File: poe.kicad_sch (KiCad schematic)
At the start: 59 parts, among them IC1 TPS2378DDA, J1 B2B-XH-A_LF__SN_, J6 SS-74800-144, U3 TPS2373-3RGW, U4 URB4805YMD-30WR3

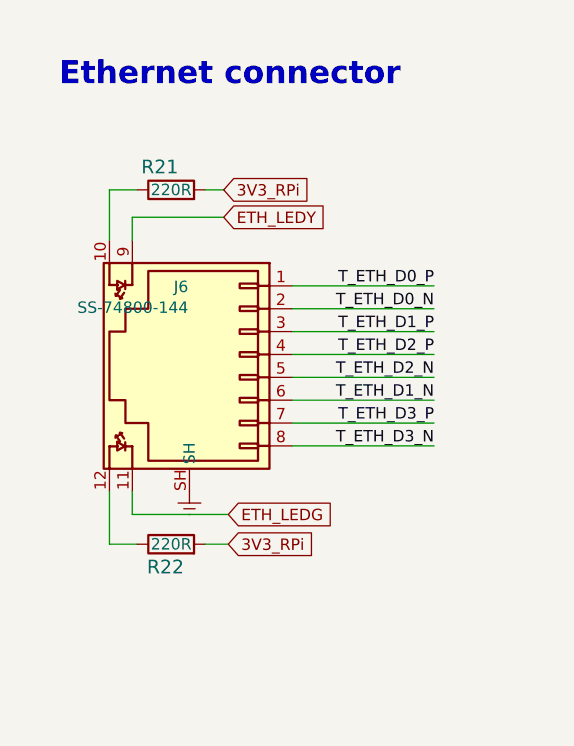
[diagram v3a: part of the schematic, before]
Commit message: Update R21, R22, R56, R57, R60, R61 symbol and footprints
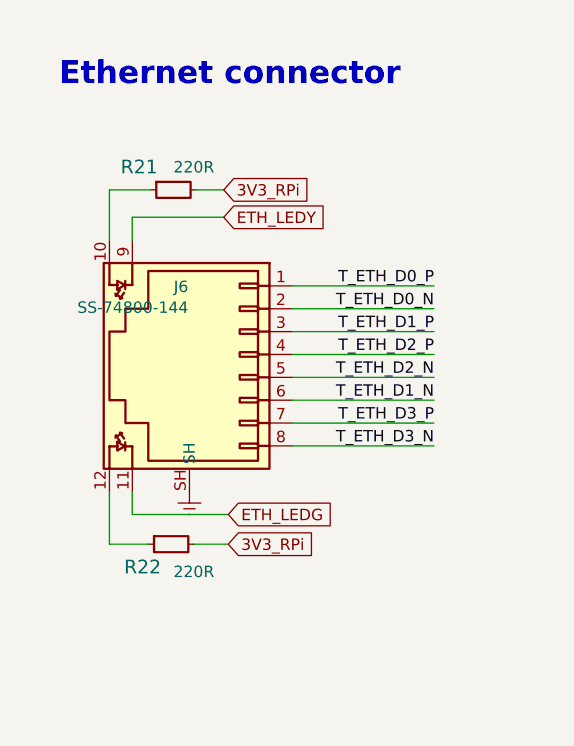
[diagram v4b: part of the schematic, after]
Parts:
- R21, R22: footprint scalenode-cm4-baseboard-footprints:0402-res -> antmicro-footprints:R_0402_1005Metric; symbol scalenode-cm4-baseboard:R_220R_0402 -> antmicroResistors0402:R_220R_0402; Author (none) -> Antmicro; License (none) -> Apache-2.0; MPN ERJ2GEJ221X -> CR0402-FX-2200GLF; Manufacturer Panasonic -> Bourns; Tolerance (none) -> 1%
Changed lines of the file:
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@@
     (stroke (width 0) (type default) (color 0 0 0 0))
   )
-  (wire (pts (xy 53.594 62.23) (xy 50.546 62.23))
+  (wire (pts (xy 50.546 62.23) (xy 55.118 62.23))
     (stroke (width 0) (type default) (color 0 0 0 0))
   )
@@
     (stroke (width 0) (type default) (color 0 0 0 0))
   )
-  (wire (pts (xy 50.546 101.6) (xy 53.594 101.6))
+  (wire (pts (xy 50.546 101.6) (xy 54.864 101.6))
     (stroke (width 0) (type default) (color 0 0 0 0))
   )
@@
     (stroke (width 0) (type default) (color 0 0 0 0))
   )
-  (wire (pts (xy 61.214 62.23) (xy 63.246 62.23))
+  (wire (pts (xy 60.198 62.23) (xy 63.246 62.23))
     (stroke (width 0) (type default) (color 0 0 0 0))
   )
@@
     (stroke (width 0) (type default) (color 0 0 0 0))
   )
-  (wire (pts (xy 61.214 101.6) (xy 63.754 101.6))
+  (wire (pts (xy 59.944 101.6) (xy 63.754 101.6))
     (stroke (width 0) (type default) (color 0 0 0 0))
   )
@@
     )
   )
-  (symbol (lib_id "scalenode-cm4-baseboard:R_220R_0402") (at 57.404 62.23 0) (unit 1)
+  (symbol (lib_id "antmicroResistors0402:R_220R_0402") (at 55.118 62.23 0) (unit 1)
     (in_bom yes) (on_board yes)
-    (property "Reference" "R21" (id 0) (at 56.134 59.69 0)
+    (property "Reference" "R21" (id 0) (at 53.848 59.69 0)
       (effects (font (size 1.524 1.524)))
     )
-    (property "Value" "R_220R_0402" (id 1) (at 57.404 66.04 0)
+    (property "Value" "R_220R_0402" (id 1) (at 55.118 66.04 0)
       (effects (font (size 1.524 1.524)) hide)
     )
-    (property "Footprint" "scalenode-cm4-baseboard-footprints:0402-res" (id 2) (at 62.484 57.15 0)
-      (effects (font (size 1.524 1.524)) (justify left) hide)
+    (property "Footprint" "antmicro-footprints:R_0402_1005Metric" (id 2) (at 75.438 77.47 0)
+      (effects (font (size 1.27 1.27) (thickness 0.15)) (justify left bottom) hide)
     )
-    (property "Datasheet" "" (id 3) (at 57.404 62.23 0)
-      (effects (font (size 1.27 1.27)) hide)
+    (property "Datasheet" "https://www.bourns.com/docs/product-datasheets/cr.pdf" (id 3) (at 75.438 80.01 0)
+      (effects (font (size 1.27 1.27) (thickness 0.15)) (justify left bottom) hide)
+    )
+    (property "Manufacturer" "Bourns" (id 4) (at 75.438 85.09 0)
+      (effects (font (size 1.27 1.27) (thickness 0.15)) (justify left bottom) hide)
+    )
+    (property "MPN" "CR0402-FX-2200GLF" (id 5) (at 75.438 82.55 0)
+      (effects (font (size 1.27 1.27) (thickness 0.15)) (justify left bottom) hide)
+    )
+    (property "Val" "220R" (id 6) (at 57.658 60.452 0)
+      (effects (font (size 1.27 1.27) (thickness 0.15)) (justify left bottom))
+    )
+    (property "License" "Apache-2.0" (id 7) (at 75.438 87.63 0)
+      (effects (font (size 1.27 1.27) (thickness 0.15)) (justify left bottom) hide)
     )
-    (property "Manufacturer" "Panasonic" (id 4) (at 62.484 52.07 0)
-      (effects (font (size 1.524 1.524)) (justify left) hide)
+    (property "Author" "Antmicro" (id 8) (at 75.438 90.17 0)
+      (effects (font (size 1.27 1.27) (thickness 0.15)) (justify left bottom) hide)
     )
-    (property "MPN" "ERJ2GEJ221X" (id 5) (at 62.484 54.61 0)
-      (effects (font (size 1.524 1.524)) (justify left) hide)
+    (property "Tolerance" "1%" (id 9) (at 75.438 72.39 0)
+      (effects (font (size 1.27 1.27)) (justify left bottom) hide)
     )
-    (property "Val" "220R" (id 6) (at 57.404 62.23 0))
     (pin "1")
     (pin "2")
   )
-  (symbol (lib_id "scalenode-cm4-baseboard:R_220R_0402") (at 57.404 101.6 0) (unit 1)
+  (symbol (lib_id "antmicroResistors0402:R_220R_0402") (at 54.864 101.6 0) (unit 1)
     (in_bom yes) (on_board yes)
-    (property "Reference" "R22" (id 0) (at 56.769 104.14 0)
+    (property "Reference" "R22" (id 0) (at 54.229 104.14 0)
       (effects (font (size 1.524 1.524)))
     )
-    (property "Value" "R_220R_0402" (id 1) (at 57.404 105.41 0)
+    (property "Value" "R_220R_0402" (id 1) (at 54.864 105.41 0)
       (effects (font (size 1.524 1.524)) hide)
     )
-    (property "Footprint" "scalenode-cm4-baseboard-footprints:0402-res" (id 2) (at 62.484 96.52 0)
-      (effects (font (size 1.524 1.524)) (justify left) hide)
+    (property "Footprint" "antmicro-footprints:R_0402_1005Metric" (id 2) (at 75.184 116.84 0)
+      (effects (font (size 1.27 1.27) (thickness 0.15)) (justify left bottom) hide)
     )
-    (property "Datasheet" "" (id 3) (at 57.404 101.6 0)
-      (effects (font (size 1.27 1.27)) hide)
+    (property "Datasheet" "https://www.bourns.com/docs/product-datasheets/cr.pdf" (id 3) (at 75.184 119.38 0)
+      (effects (font (size 1.27 1.27) (thickness 0.15)) (justify left bottom) hide)
+    )
+    (property "Manufacturer" "Bourns" (id 4) (at 75.184 124.46 0)
+      (effects (font (size 1.27 1.27) (thickness 0.15)) (justify left bottom) hide)
+    )
+    (property "MPN" "CR0402-FX-2200GLF" (id 5) (at 75.184 121.92 0)
+      (effects (font (size 1.27 1.27) (thickness 0.15)) (justify left bottom) hide)
+    )
+    (property "Val" "220R" (id 6) (at 57.658 105.41 0)
+      (effects (font (size 1.27 1.27) (thickness 0.15)) (justify left bottom))
+    )
+    (property "License" "Apache-2.0" (id 7) (at 75.184 127 0)
+      (effects (font (size 1.27 1.27) (thickness 0.15)) (justify left bottom) hide)
     )
-    (property "Manufacturer" "Panasonic" (id 4) (at 62.484 91.44 0)
-      (effects (font (size 1.524 1.524)) (justify left) hide)
+    (property "Author" "Antmicro" (id 8) (at 75.184 129.54 0)
+      (effects (font (size 1.27 1.27) (thickness 0.15)) (justify left bottom) hide)
     )
-    (property "MPN" "ERJ2GEJ221X" (id 5) (at 62.484 93.98 0)
-      (effects (font (size 1.524 1.524)) (justify left) hide)
+    (property "Tolerance" "1%" (id 9) (at 75.184 111.76 0)
+      (effects (font (size 1.27 1.27)) (justify left bottom) hide)
     )
-    (property "Val" "220R" (id 6) (at 57.404 101.6 0))
     (pin "1")
     (pin "2")

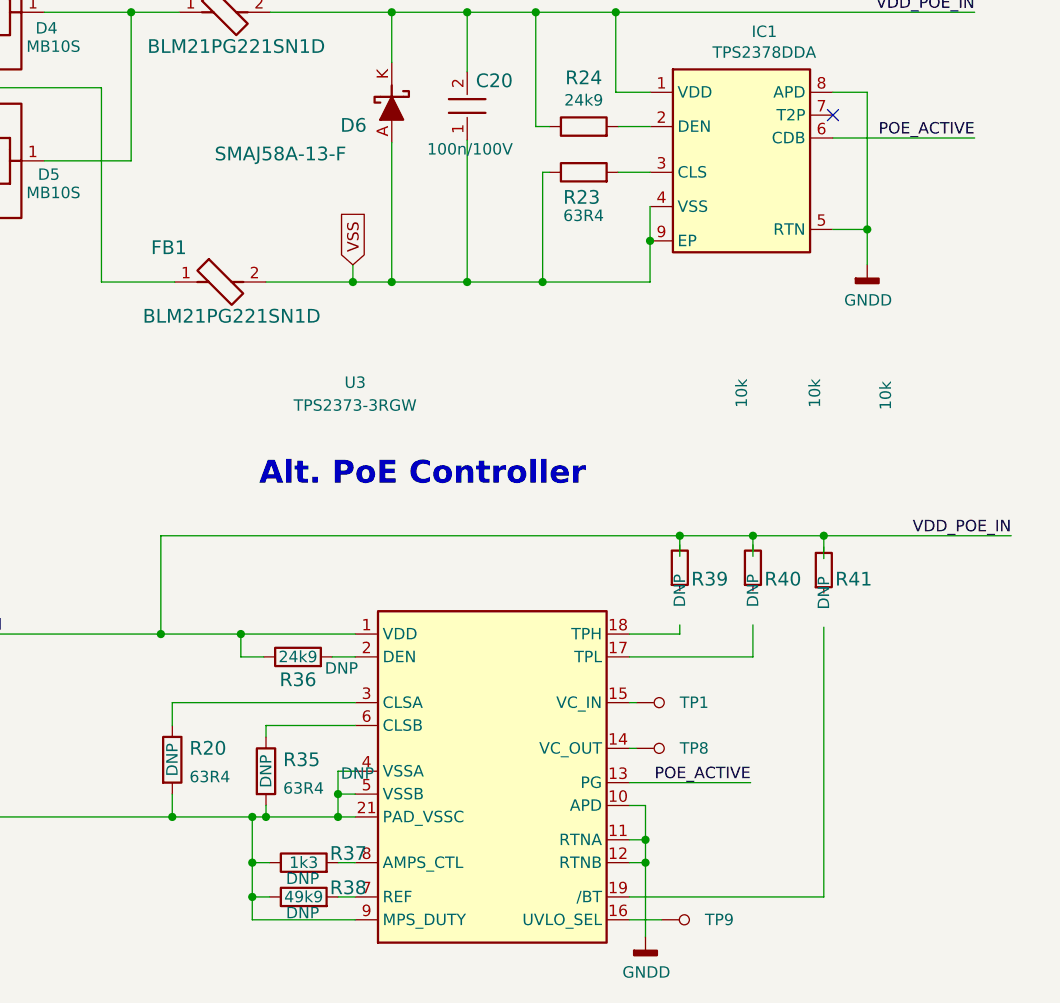
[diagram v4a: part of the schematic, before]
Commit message: Update R20 R23 R35 symbol and footprint
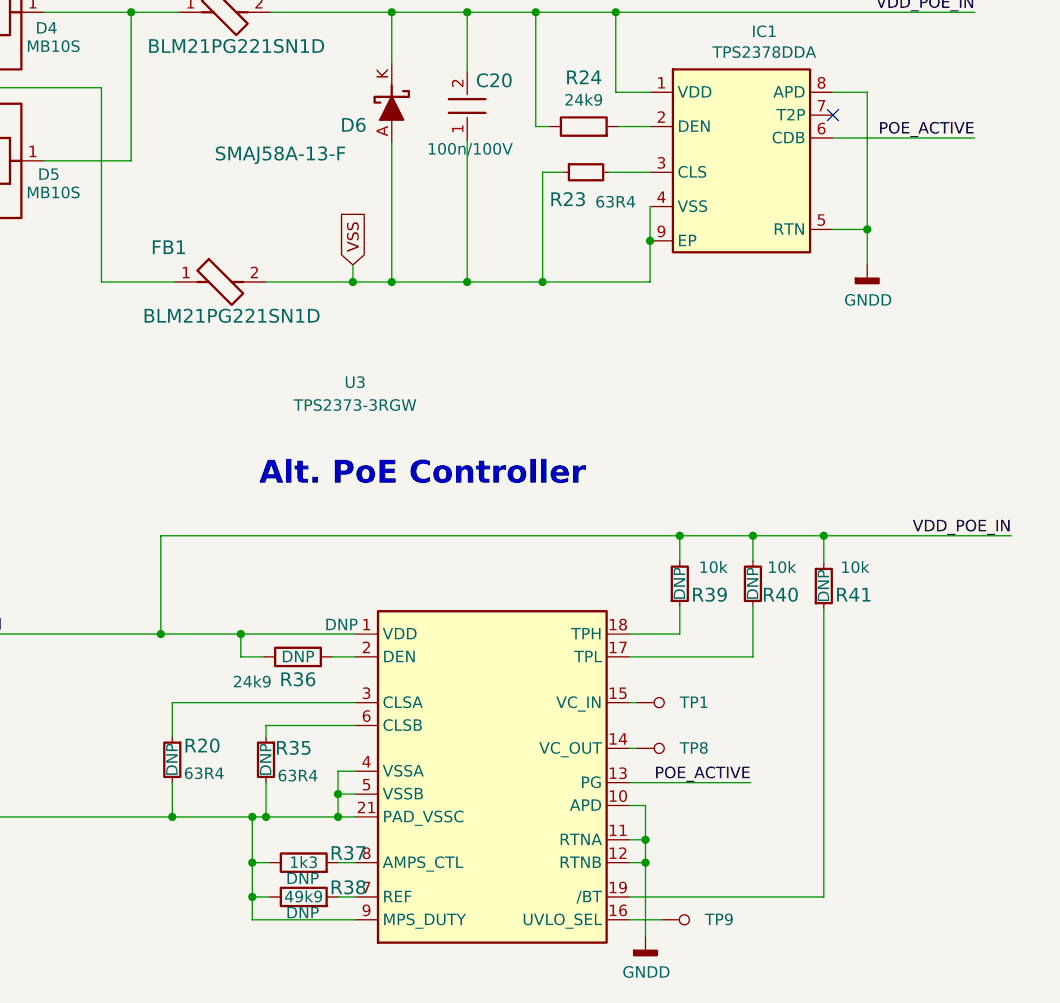
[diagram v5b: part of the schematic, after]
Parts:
- R20, R35: footprint scalenode-cm4-baseboard-footprints:0402-res -> antmicro-footprints:R_0402_1005Metric; symbol scalenode-cm4-baseboard:R_63R4_0402 -> antmicroResistors0402:R_63R4_0402; Author (none) -> Antmicro; License (none) -> Apache-2.0; MPN CRCW040263R4FKED -> CR0402-FX-63R4GLF; Manufacturer Vishay -> Bourns; Tolerance (none) -> 1%; now in the parts list
- R23: footprint scalenode-cm4-baseboard-footprints:0402-res -> antmicro-footprints:R_0402_1005Metric; symbol scalenode-cm4-baseboard:R_63R4_0402 -> antmicroResistors0402:R_63R4_0402; Author (none) -> Antmicro; License (none) -> Apache-2.0; MPN CRCW040263R4FKED -> CR0402-FX-63R4GLF; Manufacturer Vishay -> Bourns; Tolerance (none) -> 1%
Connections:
- net VDD_POE_IN: now also R39.2, R40.2, R41.2
- net at U3.17 (TPL): now also R40.1
- net at U3.18 (TPH): now also R39.1
- net at U3.19 (/BT): now also R41.1
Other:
- moved on the sheet: R35, R39, R40, R41

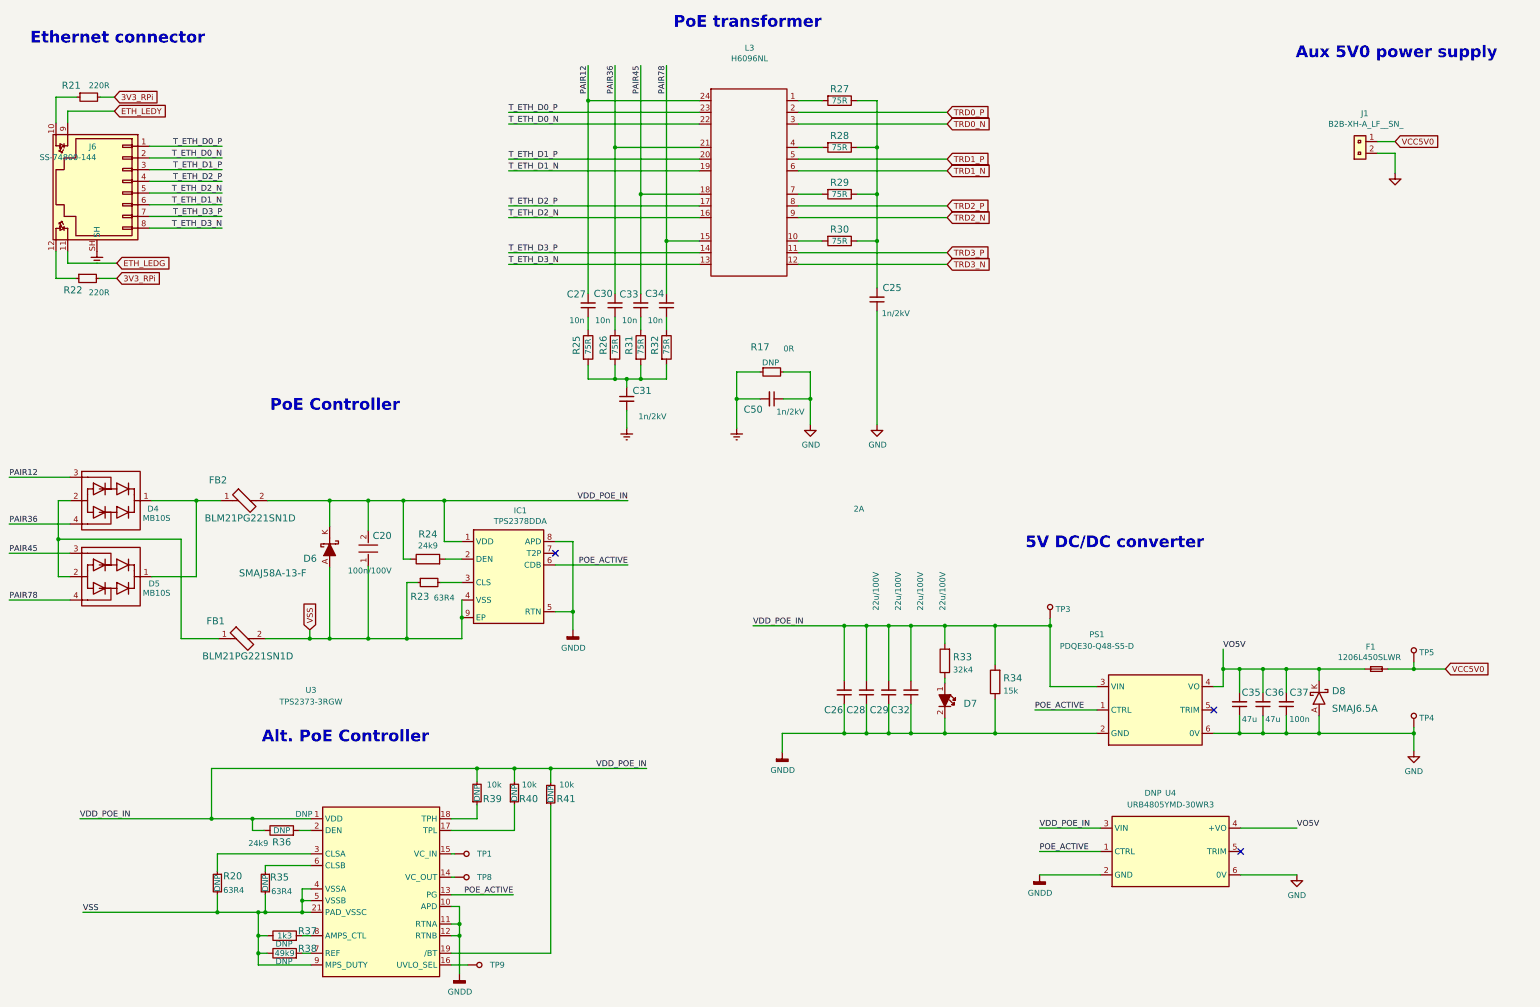
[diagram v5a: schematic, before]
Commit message: Update R25, R26, R27, R28, R29, R30, R31, R32 symbol and footprint
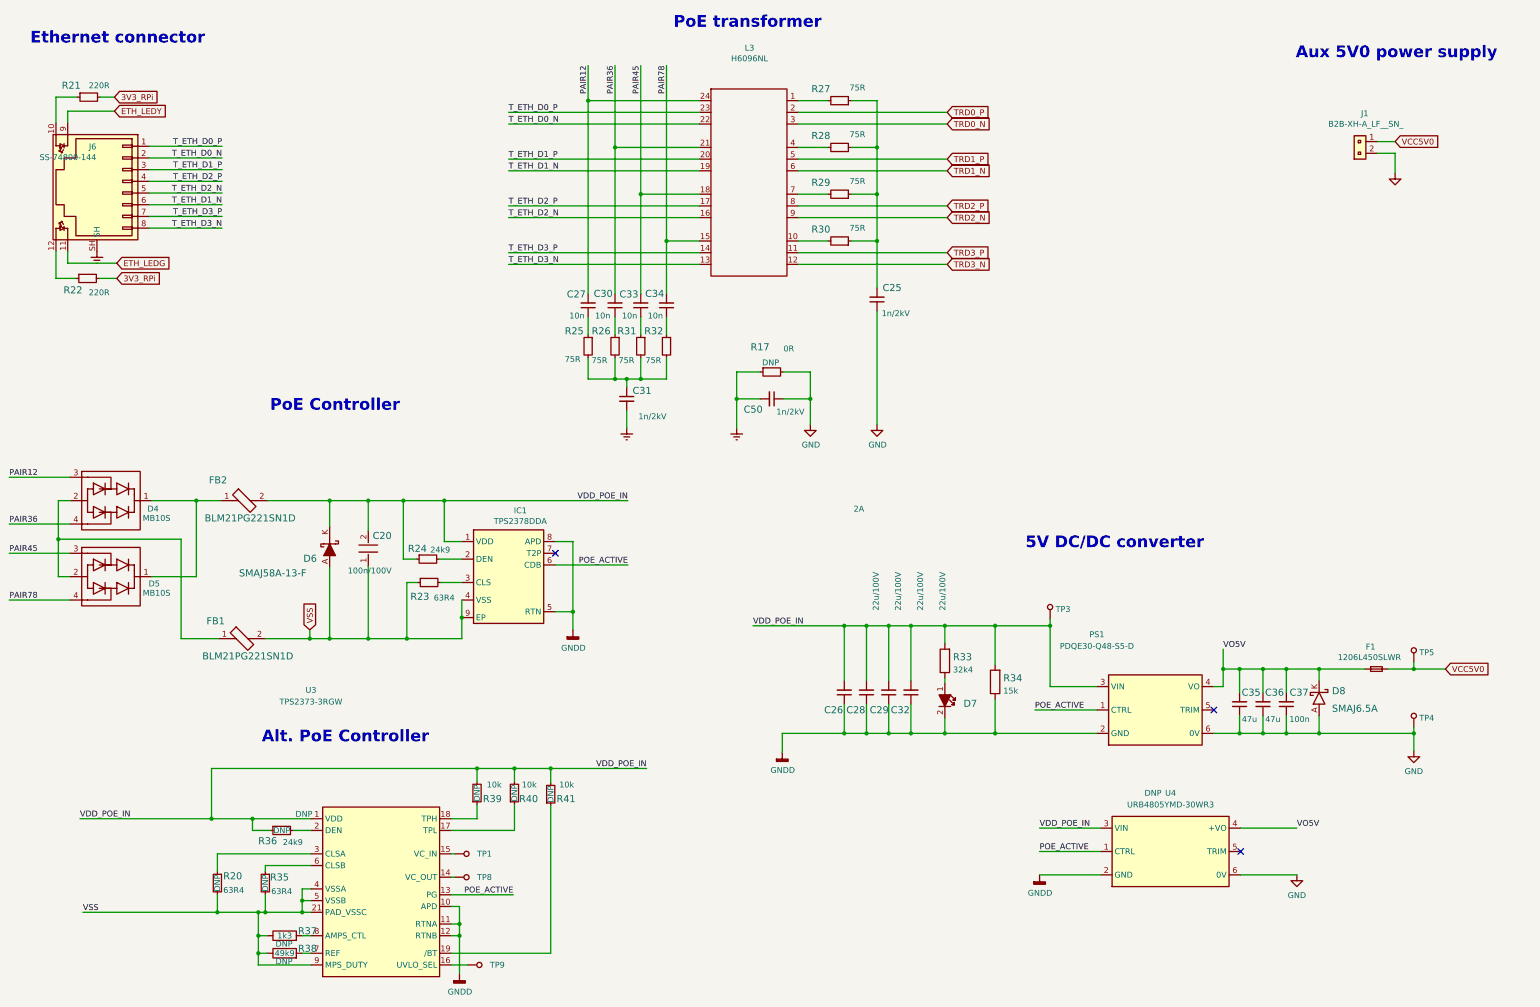
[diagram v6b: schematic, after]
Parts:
- R24: footprint scalenode-cm4-baseboard-footprints:0402-res -> antmicro-footprints:R_0402_1005Metric; symbol scalenode-cm4-baseboard:R_24k9_0402 -> antmicroResistors0402:R_24k9_0402; Author (none) -> Antmicro; License (none) -> Apache-2.0; MPN WR04X2492FTL -> CR0402-FX-2492GLF; Manufacturer WALSIN -> Bourns; Tolerance (none) -> 1%
- R25, R26, R27, R28, R29, R30, R31, R32: footprint scalenode-cm4-baseboard-footprints:0402-res -> antmicro-footprints:R_0402_1005Metric; symbol scalenode-cm4-baseboard:R_75R_0402 -> antmicroResistors0402:R_75R_0402; Author (none) -> Antmicro; License (none) -> Apache-2.0; MPN RC0402FR-0775RL -> CR0402-FX-75R0GLF; Manufacturer YAGEO -> Bourns; Tolerance (none) -> 1%
- R36: footprint scalenode-cm4-baseboard-footprints:0402-res -> antmicro-footprints:R_0402_1005Metric; symbol scalenode-cm4-baseboard:R_24k9_0402 -> antmicroResistors0402:R_24k9_0402; Author (none) -> Antmicro; License (none) -> Apache-2.0; MPN WR04X2492FTL -> CR0402-FX-2492GLF; Manufacturer WALSIN -> Bourns; Tolerance (none) -> 1%; now in the parts list
